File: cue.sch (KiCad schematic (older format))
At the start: 43 parts, among them P1 IN_1, P2 IN_2, P3 IN_3, P4 IN_4, P5 CUE, P6 CONN_01X03, SW1 DPDT_switch_4U, SW2 DPDT_switch_4U, SW3 DPDT_switch_4U, SW4 DPDT_switch_4U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

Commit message: Add LEDs references
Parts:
- D1: Description (none) -> DEL standard - Trou traversant Pink Clear 2200mcd; Distributor Digikey -> Mouser; Distributor Part # (none) -> 696-SSL-LX5093PC; Manufacturer (none) -> Lumex; Mfg_Part_# (none) -> SSL-LX5093PC; Mfg_Part_No 0 -> SSL-LX5093PC; Package 0402 -> 2-THT
- D2: Description (none) -> DEL standard - Trou traversant 5mm Thru Hole LED 592nm for 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; Distributor (none) -> Mouser; Distributor Part # (none) -> 593-LTH5MM12VFR4700; Manufacturer (none) -> VCC; Mfg_Part_# (none) -> LTH5MM12VFR4700; Package (none) -> 2-THT
- D3: Description (none) -> DEL standard - Trou traversant Turquoise Clear 2200mcd; Distributor (none) -> Mouser; Distributor Part # (none) -> 696-SSL-LX5093TC; Manufacturer (none) -> Lumex; Mfg_Part_# (none) -> SSL-LX5093TC; Package (none) -> 2-THT
- D4: Description (none) -> DEL standard - Trou traversant Red Round; Distributor (none) -> Mouser; Distributor Part # (none) -> 941-C503B-RAN-CZ0C0AA1; Manufacturer (none) -> Cree Inc.; Mfg_Part_# (none) -> C503B-RAN-CZ0C0AA1; Package (none) -> 2-THT
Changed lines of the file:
@@
 LIBS:contrib
 LIBS:valves
-LIBS:dpdt_switch_4u
-LIBS:Cue-cache
+LIBS:cue-cache
 EELAYER 25 0
 EELAYER END
@@
 F 1 "LED" H 6350 850 50  0000 C CNN
 F 2 "LEDs:LED_D5.0mm_Horizontal_O6.35mm_Z9.0mm" H 6350 950 50  0001 C CNN
-F 3 "" H 6350 950 50  0000 C CNN
-F 4 "0" H 6350 950 60  0001 C CNN "Mfg_Part_No"
-F 5 "Digikey" H 6350 950 60  0001 C CNN "Distributor"
-F 6 "0402" H 6350 950 60  0001 C CNN "Package"
+F 3 "http://www.mouser.com/ds/2/244/SSL-LX5093PC-1137578.pdf" H 6350 950 50  0001 C CNN
+F 4 "SSL-LX5093PC" H 6350 950 60  0001 C CNN "Mfg_Part_#"
+F 5 "Mouser" H 6350 950 60  0001 C CNN "Distributor"
+F 6 "696-SSL-LX5093PC" H 6350 950 60  0001 C CNN "Distributor Part #"
+F 7 "2-THT" H 6350 950 60  0001 C CNN "Package"
+F 8 "DEL standard - Trou traversant Pink Clear 2200mcd" H 6350 950 60  0001 C CNN "Description"
+F 9 "Lumex" H 6350 950 60  0001 C CNN "Manufacturer"
+F 10 "SSL-LX5093PC" H 6350 950 60  0001 C CNN "Mfg_Part_No"
 	1    6350 950
 	-1   0    0    1
@@
 F 1 "LED" H 6350 3250 50  0000 C CNN
 F 2 "LEDs:LED_D5.0mm_Horizontal_O6.35mm_Z9.0mm" H 6350 3350 50  0001 C CNN
-F 3 "" H 6350 3350 50  0000 C CNN
+F 3 "http://www.mouser.com/ds/2/423/LTH5MM12VFR4700-1099608.pdf" H 6350 3350 50  0001 C CNN
+F 4 "LTH5MM12VFR4700" H 6350 3350 60  0001 C CNN "Mfg_Part_#"
+F 5 "Mouser" H 6350 3350 60  0001 C CNN "Distributor"
+F 6 "593-LTH5MM12VFR4700" H 6350 3350 60  0001 C CNN "Distributor Part #"
+F 7 "2-THT" H 6350 3350 60  0001 C CNN "Package"
+F 8 "DEL standard - Trou traversant 5mm Thru Hole LED 592nm for 12VDC" H 6350 3350 60  0001 C CNN "Description"
+F 9 "VCC" H 6350 3350 60  0001 C CNN "Manufacturer"
 	1    6350 3350
 	-1   0    0    1
@@
 F 1 "LED" H 9950 850 50  0000 C CNN
 F 2 "LEDs:LED_D5.0mm_Horizontal_O6.35mm_Z9.0mm" H 9950 950 50  0001 C CNN
-F 3 "" H 9950 950 50  0000 C CNN
+F 3 "http://www.mouser.com/ds/2/244/SSL-LX5093TC-1137433.pdf" H 9950 950 50  0001 C CNN
+F 4 "SSL-LX5093TC" H 9950 950 60  0001 C CNN "Mfg_Part_#"
+F 5 "Mouser" H 9950 950 60  0001 C CNN "Distributor"
+F 6 "696-SSL-LX5093TC" H 9950 950 60  0001 C CNN "Distributor Part #"
+F 7 "2-THT" H 9950 950 60  0001 C CNN "Package"
+F 8 "DEL standard - Trou traversant Turquoise Clear 2200mcd" H 9950 950 60  0001 C CNN "Description"
+F 9 "Lumex" H 9950 950 60  0001 C CNN "Manufacturer"
 	1    9950 950
 	-1   0    0    1
@@
 F 1 "LED" H 9950 3250 50  0000 C CNN
 F 2 "LEDs:LED_D5.0mm_Horizontal_O6.35mm_Z9.0mm" H 9950 3350 50  0001 C CNN
-F 3 "" H 9950 3350 50  0000 C CNN
+F 3 "http://www.mouser.com/ds/2/90/C503B%20RAS%20RAN%20AAS%20AAN%20RBS%20RBN%20ABS%20ABN%20RCS%20RCN%20ACS%20-269115.pdf" H 9950 3350 50  0001 C CNN
+F 4 "C503B-RAN-CZ0C0AA1" H 9950 3350 60  0001 C CNN "Mfg_Part_#"
+F 5 "Mouser" H 9950 3350 60  0001 C CNN "Distributor"
+F 6 "941-C503B-RAN-CZ0C0AA1" H 9950 3350 60  0001 C CNN "Distributor Part #"
+F 7 "2-THT" H 9950 3350 60  0001 C CNN "Package"
+F 8 "DEL standard - Trou traversant Red Round" H 9950 3350 60  0001 C CNN "Description"
+F 9 "Cree Inc." H 9950 3350 60  0001 C CNN "Manufacturer"
 	1    9950 3350
 	-1   0    0    1

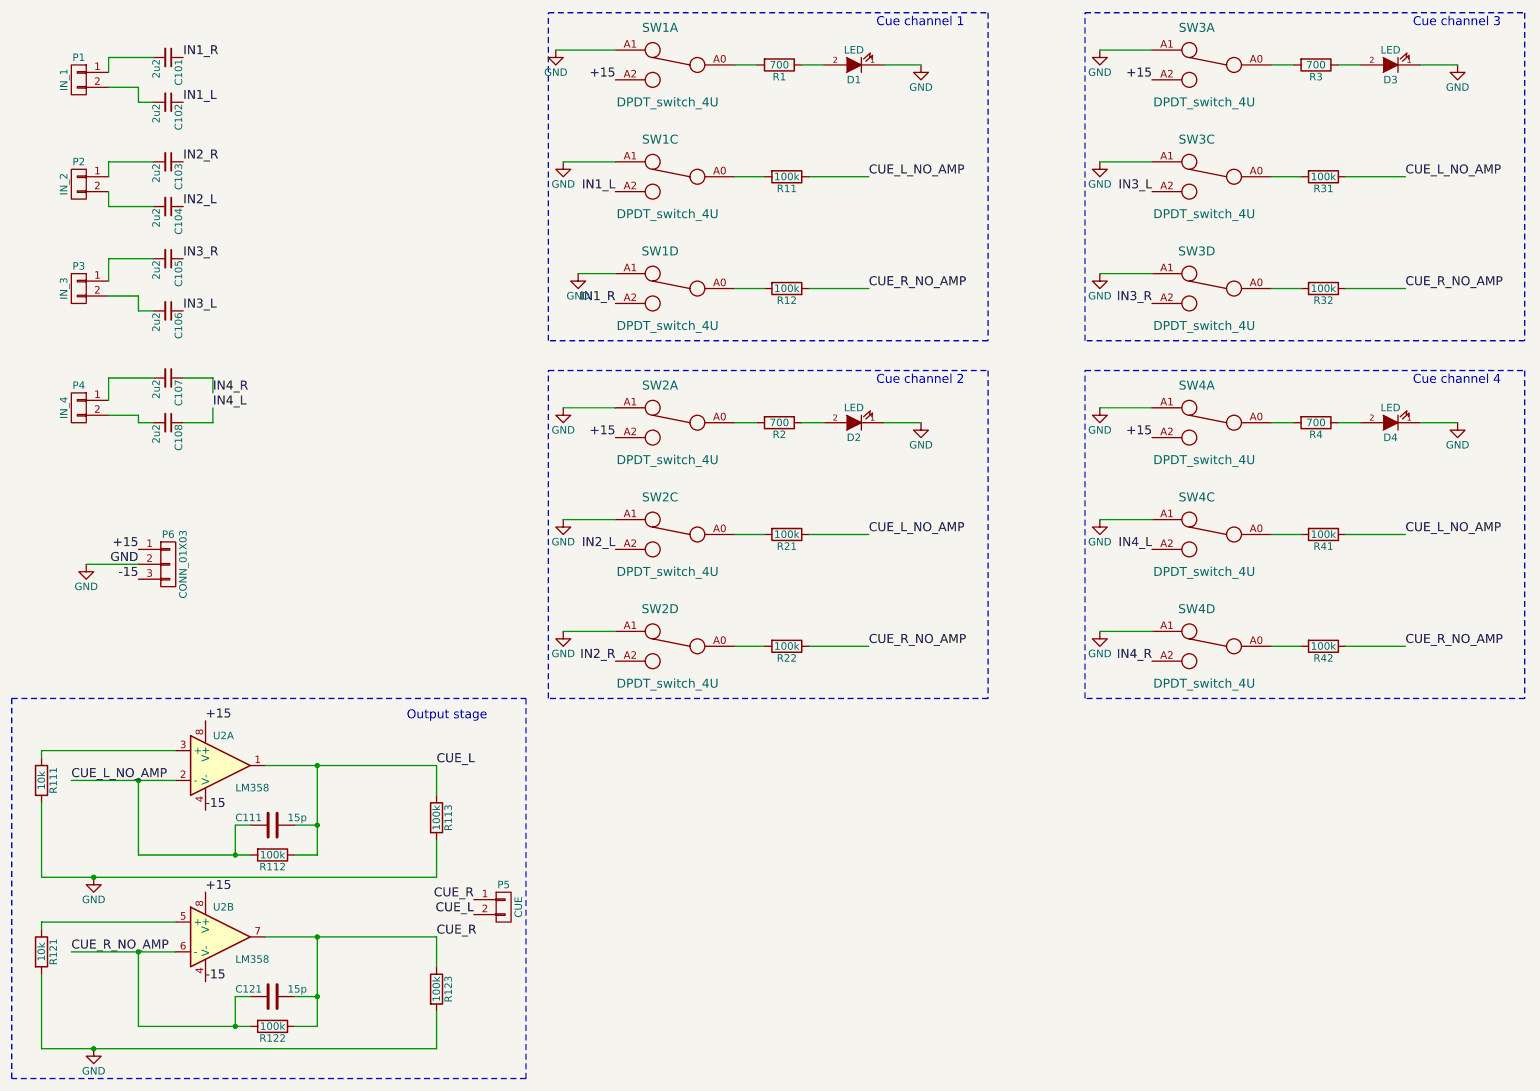
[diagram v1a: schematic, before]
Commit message: Add components references
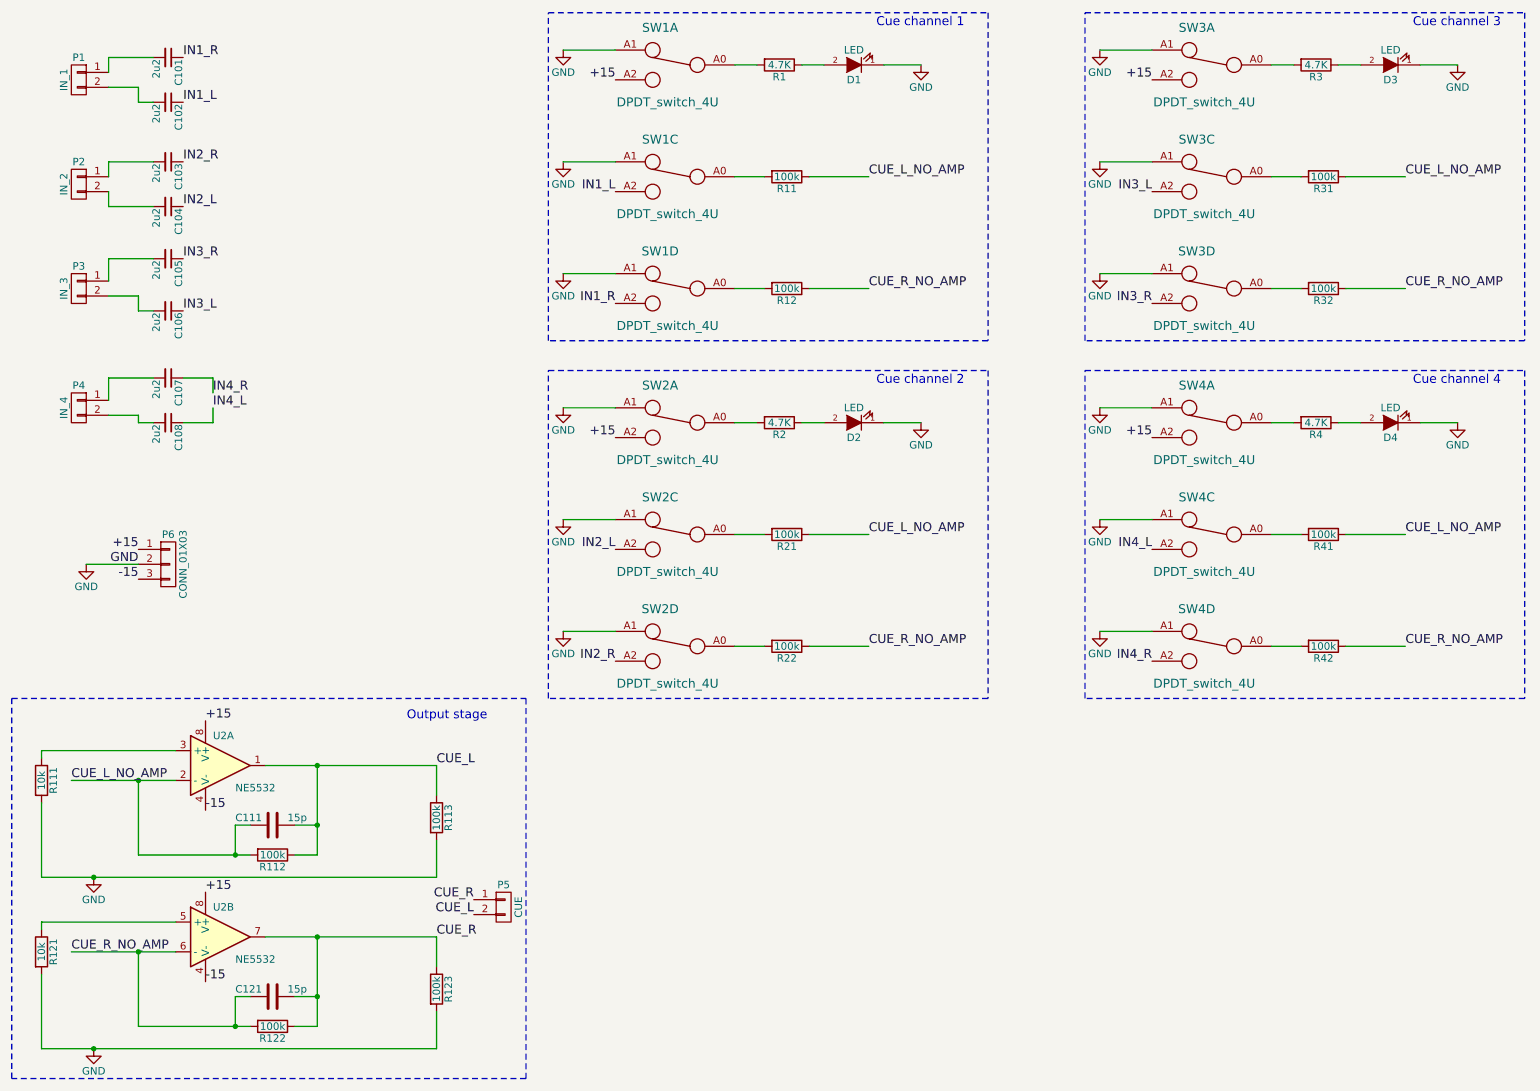
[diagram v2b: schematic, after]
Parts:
- C101, C102, C103, C104, C105, C106, C107, C108: Distributor (none) -> Mouser; Mfg_Part_# (none) -> RSBCC4220Z310K; Mouser Digikey -> (none); Package 0402 -> 2-THT
- C111, C121: Description (none) -> Condensateurs céramique multicouches MLCC - Traversant 15pF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; Distributor (none) -> Mouser; Distributor Part # (none) -> 594-K150J15C0GF5TL2; Manufacturer (none) -> Vishay / BC Components; Mfg_Part_# (none) -> K150J15C0GF5TL2; Package (none) -> 2-THT
- R1, R2, R3, R4: value 700 -> 4.7K; Description (none) -> Résistances à couche mince - Trou traversant .4watt 4.7Kohm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; Distributor (none) -> Mouser; Distributor Part # (none) -> 594-5063JD4K700F; Manufacturer (none) -> Vishay / BC Components; Mfg_Part_# (none) -> MBA02040C4701FC100; Package (none) -> 2-THT
- R11, R112, R113, R12, R122, R123, R21, R22, R31, R32, R41, R42: Description (none) -> Résistances à couche métallique - Trou traversant 1/3watts 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; Distributor (none) -> Mouser; Distributor Part # (none) -> 71-CCF50-100K; Manufacturer (none) -> Vishay / Dale; Mfg_Part_# (none) -> CCF50100KFKR36; Package (none) -> 2-THT
- R111, R121: Description (none) -> Résistances à couche métallique - Trou traversant 1/3watts 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; Distributor (none) -> Mouser; Distributor Part # (none) -> 71-CCF5010K0FKE36; Manufacturer (none) -> Vishay / Dale; Mfg_Part_# (none) -> CCF5010K0FKE36; Package (none) -> 2-THT
- SW1, SW2, SW3, SW4: Description (none) -> Pushbutton Switches PB SWITCH; Distributor Digikey -> Mouser; Distributor Part # (none) -> 611-F4UEE; Manufacturer (none) -> C&K Components; Mfg_Part_# (none) -> F4UEE; Mfg_Part_No 0 -> F4UEE; Package 0402 -> 12-THT
- SW1, SW2, SW3, SW4: Mfg_Part_# (none) -> F4UEE; Package 0402 -> 12-THT
- U2: value LM358 -> NE5532; Description (none) -> Amplificateurs opérationnels - Amplis-Op Dual Low Noise; Distributor (none) -> Mouser; Distributor Part # (none) -> 595-NE5532P; Manufacturer (none) -> Texas Instruments; Mfg_Part_# (none) -> NE5532P; Package (none) -> 8-PDIP
